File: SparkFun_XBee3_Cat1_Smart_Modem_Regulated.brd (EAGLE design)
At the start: 35.6 x 52.1 mm, 96 parts, among them J4 QWIIC_RIGHT_ANGLE, U2 AP63203

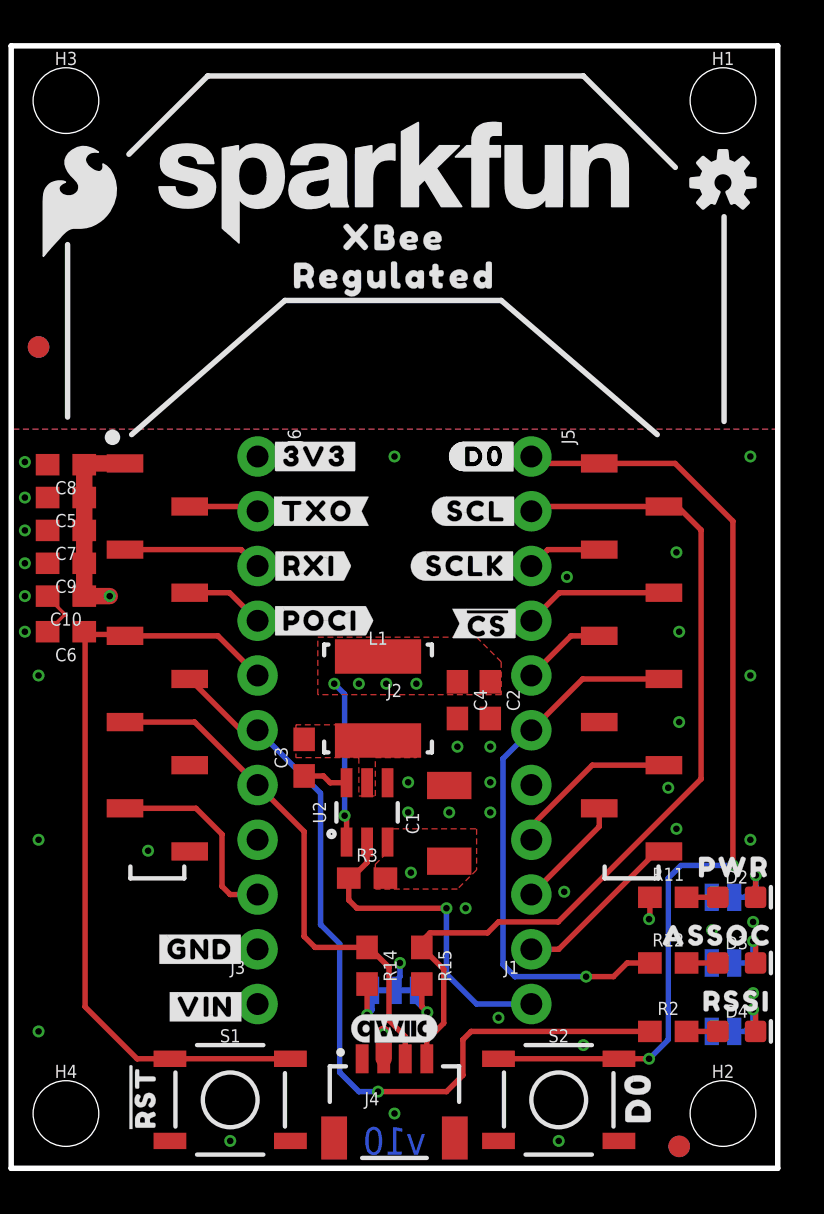
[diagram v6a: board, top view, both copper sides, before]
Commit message: Moves some silk around
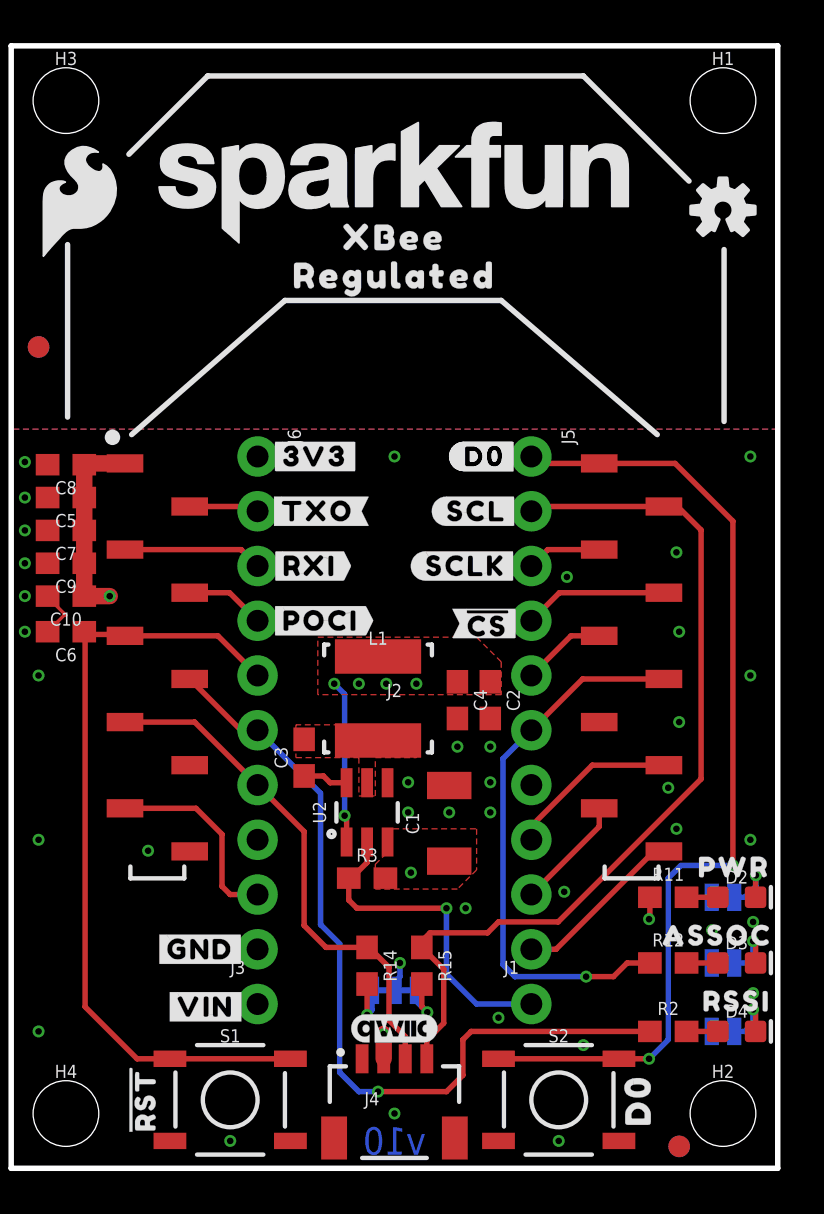
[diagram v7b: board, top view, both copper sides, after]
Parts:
- moved LOGO4 57.1 mm to (-10.2, -27.9)
- moved LOGO2 1.27 mm to (31.8, 44.5)
- moved U$30 0.13 mm to (4.83, 3.17)
- moved U$40 0.13 mm to (27.8, 3.17)
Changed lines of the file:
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@@
 <layer number="37" name="tTest" color="7" fill="1" visible="no" active="yes"/>
 <layer number="38" name="bTest" color="7" fill="1" visible="no" active="yes"/>
-<layer number="39" name="tKeepout" color="4" fill="11" visible="yes" active="yes"/>
+<layer number="39" name="tKeepout" color="4" fill="11" visible="no" active="yes"/>
 <layer number="40" name="bKeepout" color="1" fill="11" visible="no" active="yes"/>
 <layer number="41" name="tRestrict" color="4" fill="10" visible="no" active="yes"/>
@@
 <layer number="45" name="Holes" color="7" fill="1" visible="yes" active="yes"/>
 <layer number="46" name="Milling" color="3" fill="1" visible="no" active="yes"/>
-<layer number="47" name="Measures" color="7" fill="1" visible="yes" active="yes"/>
+<layer number="47" name="Measures" color="7" fill="1" visible="no" active="yes"/>
 <layer number="48" name="Document" color="7" fill="1" visible="no" active="yes"/>
 <layer number="49" name="Reference" color="13" fill="1" visible="yes" active="yes"/>
@@
 <layer number="115" name="ReferenceISLANDS" color="7" fill="1" visible="no" active="yes"/>
 <layer number="116" name="Patch_BOT" color="9" fill="4" visible="no" active="yes"/>
-<layer number="117" name="PM_Ref" color="26" fill="1" visible="yes" active="yes"/>
+<layer number="117" name="PM_Ref" color="26" fill="1" visible="no" active="yes"/>
 <layer number="118" name="Rect_Pads" color="7" fill="1" visible="no" active="yes"/>
-<layer number="119" name="PF_Ref" color="31" fill="1" visible="yes" active="yes"/>
-<layer number="120" name="WFL_Ref" color="25" fill="1" visible="yes" active="yes"/>
+<layer number="119" name="PF_Ref" color="31" fill="1" visible="no" active="yes"/>
+<layer number="120" name="WFL_Ref" color="25" fill="1" visible="no" active="yes"/>
 <layer number="121" name="_tsilk" color="7" fill="1" visible="no" active="yes"/>
 <layer number="122" name="_bsilk" color="7" fill="1" visible="no" active="yes"/>
@@
 <wire x1="4.191" y1="47.0408" x2="7.8486" y2="50.673" width="0.254" layer="21"/>
 <wire x1="7.8486" y1="50.673" x2="25.273" y2="50.673" width="0.254" layer="21"/>
-<wire x1="25.273" y1="50.673" x2="29.5402" y2="46.4312" width="0.254" layer="21"/>
-<wire x1="31.8008" y1="44.1452" x2="31.8008" y2="34.6456" width="0.254" layer="21"/>
+<wire x1="25.273" y1="50.673" x2="30.1752" y2="45.7962" width="0.254" layer="21"/>
+<wire x1="31.8008" y1="42.6212" x2="31.8008" y2="34.6456" width="0.254" layer="21"/>
 <dimension x1="10.16" y1="7.62" x2="10.16" y2="0" x3="-8.89" y3="3.81" textsize="1.778" textratio="15" layer="47" unit="inch"/>
 <dimension x1="1.27" y1="49.53" x2="-1.27" y2="49.53" x3="0" y3="53.34" textsize="1.778" textratio="15" layer="47" unit="inch"/>
@@
 <attribute name="VALUE" x="31.75" y="10.668" size="0.6096" layer="28" font="vector" ratio="20" rot="MR180" align="top-center"/>
 </element>
-<element name="LOGO2" library="SparkFun-Aesthetics" package="OSHW-LOGO-S" value="OSHW-LOGOS" x="31.75" y="45.72" smashed="yes"/>
+<element name="LOGO2" library="SparkFun-Aesthetics" package="OSHW-LOGO-S" value="OSHW-LOGOS" x="31.75" y="44.45" smashed="yes"/>
 <element name="LOGO3" library="SparkFun-Aesthetics" package="QWIIC_4MM" value="QWIIC_LOGO_4MM" x="16.51" y="6.477" smashed="yes"/>
 <element name="U2" library="SparkFun-IC-Power" package="SOT23-6" value="AP63203" x="15.24" y="16.51" smashed="yes">
@@
 <element name="U$44" library="top" package="#3V3#1" value="" x="7.493" y="33.02" smashed="yes" rot="MR0"/>
 <element name="U$46" library="top" package="#VIN#4" value="" x="7.747" y="7.493" smashed="yes" rot="MR0"/>
-<element name="U$40" library="bot" package="D03" value="" x="27.813" y="3.302" smashed="yes" rot="R90"/>
-<element name="U$30" library="top" package="#RST#30" value="" x="4.826" y="3.302" smashed="yes" rot="R90"/>
+<element name="U$40" library="bot" package="D03" value="" x="27.813" y="3.175" smashed="yes" rot="R90"/>
+<element name="U$30" library="top" package="#RST#30" value="" x="4.826" y="3.175" smashed="yes" rot="R90"/>
 <element name="U$63" library="SparkFun-Aesthetics" package="SFE_LOGO_NAME_.2" value="" x="16.51" y="45.72" smashed="yes" rot="MR0"/>
 <element name="U$61" library="SparkFun-Aesthetics" package="SFE_LOGO_FLAME_.2" value="" x="1.905" y="44.831" smashed="yes"/>
@@
 <element name="U$34" library="topmirror" package="#D3#AD3##CS##23" value="" x="28.321" y="25.273" smashed="yes" rot="MR0"/>
 <element name="LOGO1" library="SparkFun-Aesthetics" package="ORDERING_INSTRUCTIONS" value="SPECIAL_INSTRUCTIONS-ORDERING" x="45.72" y="52.07" smashed="yes"/>
-<element name="LOGO4" library="SparkFun-Aesthetics" package="BLANK" value="SFE_LOGO_NAMEBLANK" x="-30.48" y="-81.28" smashed="yes"/>
+<element name="LOGO4" library="SparkFun-Aesthetics" package="BLANK" value="SFE_LOGO_NAMEBLANK" x="-10.16" y="-27.94" smashed="yes"/>
 </elements>
 <signals>
@@
 <wire x1="4.01" y1="20.7" x2="7.24" y2="20.7" width="0.254" layer="1"/>
 <wire x1="7.24" y1="20.7" x2="10.16" y2="17.78" width="0.254" layer="1"/>
-<wire x1="15.24" y1="10.248" x2="12.827" y2="10.248" width="0.254" layer="1"/>
-<wire x1="12.827" y1="10.248" x2="12.319" y2="10.756" width="0.254" layer="1"/>
+<wire x1="15.24" y1="10.248" x2="13.335" y2="10.248" width="0.254" layer="1"/>
+<wire x1="13.335" y1="10.248" x2="12.319" y2="11.264" width="0.254" layer="1"/>
 <wire x1="12.319" y1="15.621" x2="10.16" y2="17.78" width="0.254" layer="1"/>
-<wire x1="12.319" y1="10.756" x2="12.319" y2="15.621" width="0.254" layer="1"/>
+<wire x1="12.319" y1="11.264" x2="12.319" y2="15.621" width="0.254" layer="1"/>
 <wire x1="17.01" y1="6.11303125" x2="17.01" y2="5.08" width="0.254" layer="1"/>
 <wire x1="16.256" y1="6.86703125" x2="17.01" y2="6.11303125" width="0.254" layer="1"/>
@@
 <contactref element="J2" pad="11"/>
 <contactref element="J5" pad="10"/>
-<wire x1="22.86" y1="10.16" x2="24.13" y2="10.16" width="0.254" layer="1"/>
-<wire x1="29.01" y1="14.7" x2="28.67" y2="14.7" width="0.254" layer="1"/>
-<wire x1="28.67" y1="14.7" x2="24.13" y2="10.16" width="0.254" layer="1"/>
+<wire x1="22.86" y1="10.16" x2="24.003" y2="10.16" width="0.254" layer="1"/>
+<wire x1="29.01" y1="14.7" x2="28.543" y2="14.7" width="0.254" layer="1"/>
+<wire x1="28.543" y1="14.7" x2="24.003" y2="10.16" width="0.254" layer="1"/>
 </signal>
 <signal name="D7/!CTS!">

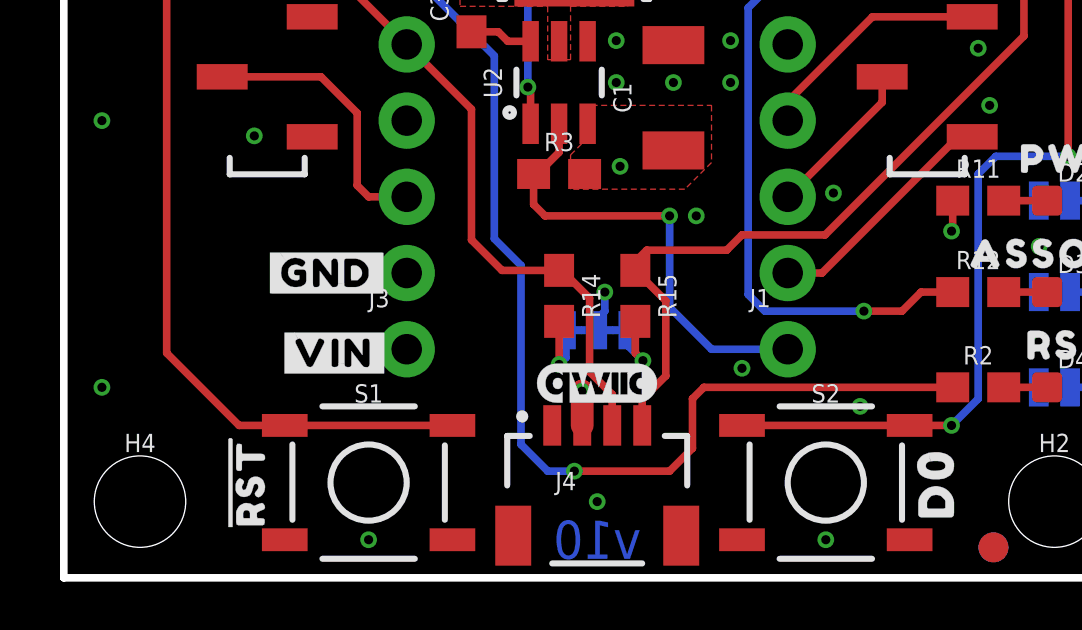
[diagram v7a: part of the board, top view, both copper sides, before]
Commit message: Adds four layer numbers, fixes accidental naming of GND to "OPEN"
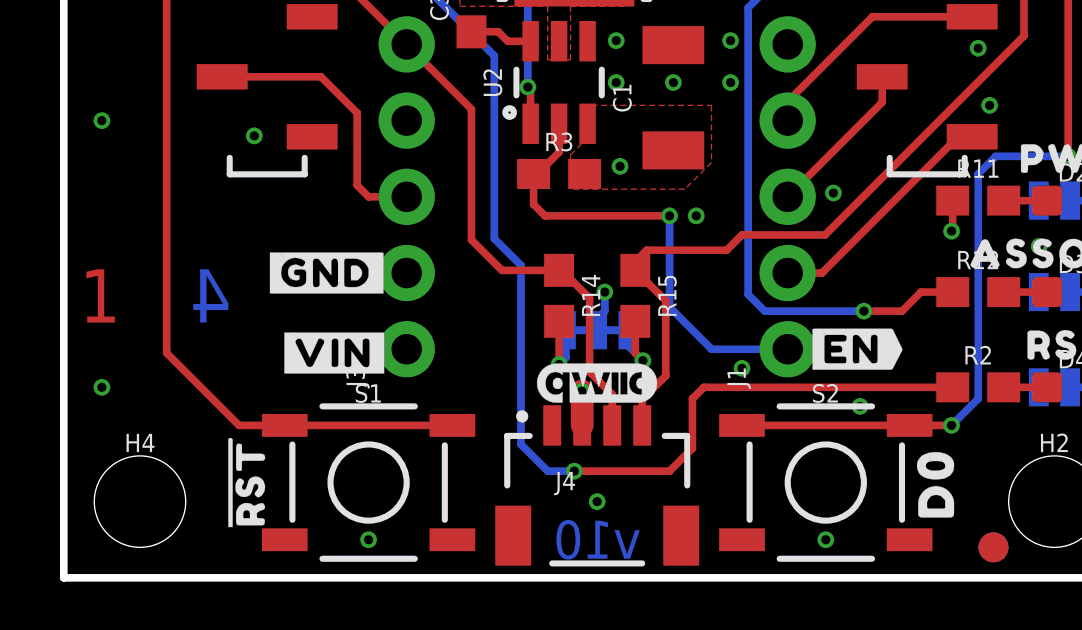
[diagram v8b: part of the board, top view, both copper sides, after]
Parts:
- added U$6: (no value), topmirror:#EN#17
- turned J1 to 90 degrees
- turned J3 to 90 degrees
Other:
- board text added: "1"
- board text added: "2"
- board text added: "3"
- board text added: "4"
